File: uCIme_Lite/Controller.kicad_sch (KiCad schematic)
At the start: 35 parts, among them J11 SERIAL_MODE, J12 SERIAL_VOLTAGE_SELECT, Q5 BSS138, Q6 BSS138, Q7 BSS138, Q8 BSS138, U3 AP2204K-ADJ, U4 AP2204K-ADJ, U5 FT230XS, U6 TXB0104D

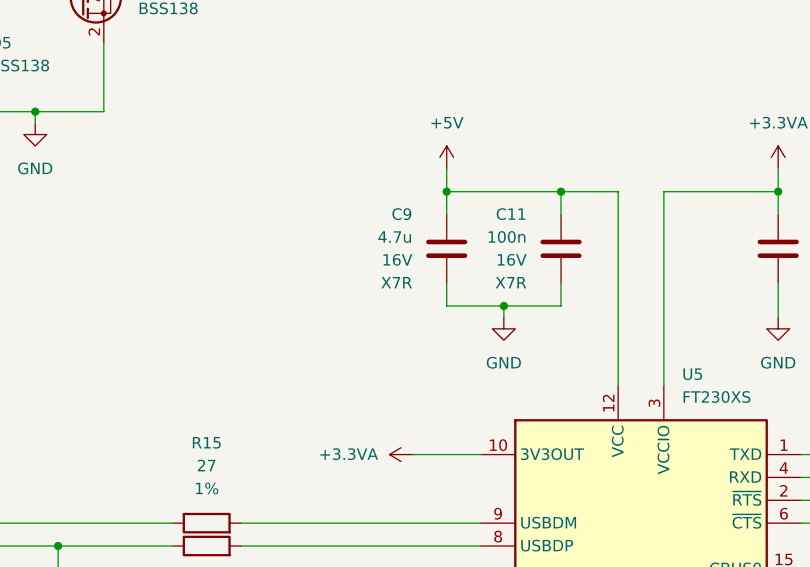
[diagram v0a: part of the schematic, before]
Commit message: lite: Added more part numbers to the schematic. Replaced the FTDI 4.7u capacitor by two 2.2u capacitors to improve the BoM.
Signed-off-by: Adrien Ricciardi <aricciardi@baylibre.com>
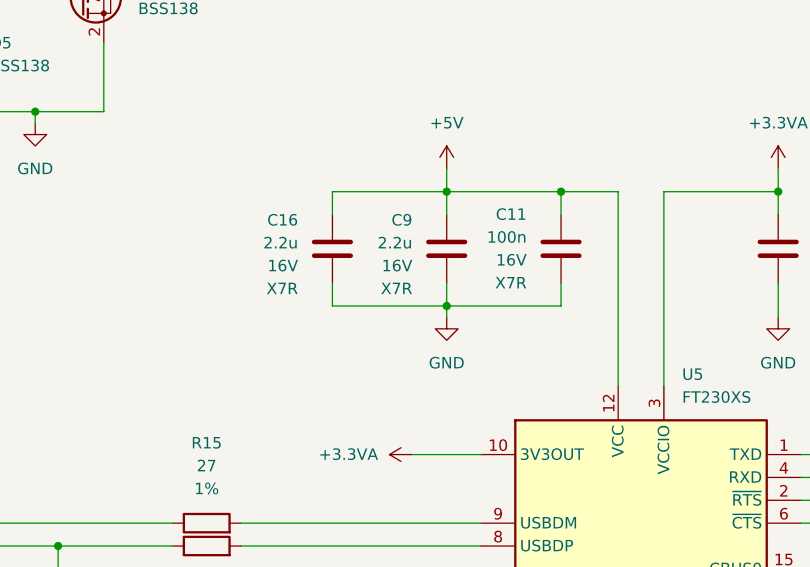
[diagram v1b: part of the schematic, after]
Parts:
- added C16: 2.2u, Capacitor_SMD:C_0603_1608Metric, symbol Device:C
- C6, C7: PartNumber (none) -> CL10C470JB81PNC
- C9: value 4.7u -> 2.2u; footprint Capacitor_SMD:C_0805_2012Metric -> Capacitor_SMD:C_0603_1608Metric; PartNumber (none) -> CL10A225KO8NNNC
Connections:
- net +5V: now also C16.1
- net GND: now also C16.2
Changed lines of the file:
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@@
   (junction (at 74.93 160.02) (diameter 0) (color 0 0 0 0)
   )
+  (junction (at 104.14 77.47) (diameter 0) (color 0 0 0 0)
+  )
   (junction (at 232.41 138.43) (diameter 0) (color 0 0 0 0)
   )
@@
   (junction (at 177.8 52.07) (diameter 0) (color 0 0 0 0)
   )
-  (junction (at 110.49 77.47) (diameter 0) (color 0 0 0 0)
-  )
   (junction (at 26.67 160.02) (diameter 0) (color 0 0 0 0)
   )
@@
     (stroke (width 0) (type default))
   )
+  (wire (pts (xy 91.44 77.47) (xy 104.14 77.47))
+    (stroke (width 0) (type default))
+  )
   (wire (pts (xy 116.84 74.93) (xy 116.84 77.47))
     (stroke (width 0) (type default))
@@
     (stroke (width 0) (type default))
   )
+  (wire (pts (xy 91.44 74.93) (xy 91.44 77.47))
+    (stroke (width 0) (type default))
+  )
   (wire (pts (xy 81.28 101.6) (xy 107.95 101.6))
     (stroke (width 0) (type default))
@@
     (stroke (width 0) (type default))
   )
-  (wire (pts (xy 110.49 77.47) (xy 110.49 78.74))
-    (stroke (width 0) (type default))
-  )
   (wire (pts (xy 36.83 160.02) (xy 26.67 160.02))
     (stroke (width 0) (type default))
@@
     (stroke (width 0) (type default))
   )
-  (wire (pts (xy 110.49 77.47) (xy 116.84 77.47))
+  (wire (pts (xy 104.14 77.47) (xy 116.84 77.47))
     (stroke (width 0) (type default))
   )
@@
     (stroke (width 0) (type default))
   )
+  (wire (pts (xy 91.44 67.31) (xy 91.44 64.77))
+    (stroke (width 0) (type default))
+  )
   (wire (pts (xy 114.3 160.02) (xy 104.14 160.02))
     (stroke (width 0) (type default))
@@
     (stroke (width 0) (type default))
   )
+  (wire (pts (xy 104.14 77.47) (xy 104.14 78.74))
+    (stroke (width 0) (type default))
+  )
   (wire (pts (xy 179.07 118.11) (xy 179.07 106.68))
     (stroke (width 0) (type default))
@@
     (stroke (width 0) (type default))
   )
-  (wire (pts (xy 104.14 77.47) (xy 110.49 77.47))
-    (stroke (width 0) (type default))
-  )
   (wire (pts (xy 58.42 55.88) (xy 58.42 57.15))
     (stroke (width 0) (type default))
@@
   )
   (wire (pts (xy 53.34 101.6) (xy 53.34 109.22))
+    (stroke (width 0) (type default))
+  )
+  (wire (pts (xy 91.44 64.77) (xy 104.14 64.77))
     (stroke (width 0) (type default))
   )
@@
       (effects (font (size 1.27 1.27)) (justify left))
     )
+    (property "PartNumber" "CL10C470JB81PNC" (at 60.96 113.03 0)
+      (effects (font (size 1.27 1.27)) hide)
+    )
     (pin "1")
     (pin "2")
@@
         (path "/6d46d15a-8cd0-4983-b142-8248cafa0b56/85cb8885-4077-4bc3-b1fe-5b247ce2fc7e"
           (reference "C7") (unit 1)
-        )
-      )
-    )
-  )
-  (symbol (lib_id "Device:C") (at 104.14 71.12 0) (unit 1)
-    (in_bom yes) (on_board yes) (dnp no) (fields_autoplaced)
-    (property "Reference" "C9" (at 100.33 67.3099 0)
-      (effects (font (size 1.27 1.27)) (justify right))
-    )
-    (property "Value" "4.7u" (at 100.33 69.8499 0)
-      (effects (font (size 1.27 1.27)) (justify right))
-    )
-    (property "Footprint" "Capacitor_SMD:C_0805_2012Metric" (at 105.1052 74.93 0)
-      (effects (font (size 1.27 1.27)) hide)
-    )
-    (property "Datasheet" "~" (at 104.14 71.12 0)
-      (effects (font (size 1.27 1.27)) hide)
-    )
-    (property "Value2" "16V" (at 100.33 72.3899 0)
-      (effects (font (size 1.27 1.27)) (justify right))
-    )
-    (property "Value3" "X7R" (at 100.33 74.9299 0)
-      (effects (font (size 1.27 1.27)) (justify right))
-    )
-    (pin "1")
-    (pin "2")
-    (instances
-      (project "uCIme_Lite"
-        (path "/6d46d15a-8cd0-4983-b142-8248cafa0b56/85cb8885-4077-4bc3-b1fe-5b247ce2fc7e"
-          (reference "C9") (unit 1)
         )
       )
@@
     )
   )
-  (symbol (lib_id "power:GND") (at 110.49 78.74 0) (unit 1)
-    (in_bom yes) (on_board yes) (dnp no) (fields_autoplaced)
-    (property "Reference" "#PWR0151" (at 110.49 85.09 0)
-      (effects (font (size 1.27 1.27)) hide)
-    )
-    (property "Value" "GND" (at 110.49 83.82 0)
-      (effects (font (size 1.27 1.27)))
-    )
-    (property "Footprint" "" (at 110.49 78.74 0)
-      (effects (font (size 1.27 1.27)) hide)
-    )
-    (property "Datasheet" "" (at 110.49 78.74 0)
+  (symbol (lib_id "power:GND") (at 104.14 78.74 0) (unit 1)
+    (in_bom yes) (on_board yes) (dnp no) (fields_autoplaced)
+    (property "Reference" "#PWR0151" (at 104.14 85.09 0)
+      (effects (font (size 1.27 1.27)) hide)
+    )
+    (property "Value" "GND" (at 104.14 83.82 0)
+      (effects (font (size 1.27 1.27)))
+    )
+    (property "Footprint" "" (at 104.14 78.74 0)
+      (effects (font (size 1.27 1.27)) hide)
+    )
+    (property "Datasheet" "" (at 104.14 78.74 0)
       (effects (font (size 1.27 1.27)) hide)
     )
@@
     (property "Value3" "X7R" (at 49.53 116.8399 0)
       (effects (font (size 1.27 1.27)) (justify right))
+    )
+    (property "PartNumber" "CL10C470JB81PNC" (at 53.34 113.03 0)
+      (effects (font (size 1.27 1.27)) hide)
     )
     (pin "1")
@@
     )
   )
+  (symbol (lib_id "Device:C") (at 104.14 71.12 0) (unit 1)
+    (in_bom yes) (on_board yes) (dnp no) (fields_autoplaced)
+    (property "Reference" "C9" (at 100.33 67.945 0)
+      (effects (font (size 1.27 1.27)) (justify right))
+    )
+    (property "Value" "2.2u" (at 100.33 70.485 0)
+      (effects (font (size 1.27 1.27)) (justify right))
+    )
+    (property "Footprint" "Capacitor_SMD:C_0603_1608Metric" (at 105.1052 74.93 0)
+      (effects (font (size 1.27 1.27)) hide)
+    )
+    (property "Datasheet" "~" (at 104.14 71.12 0)
+      (effects (font (size 1.27 1.27)) hide)
+    )
+    (property "Value2" "16V" (at 100.33 73.025 0)
+      (effects (font (size 1.27 1.27)) (justify right))
+    )
+    (property "Value3" "X7R" (at 100.33 75.565 0)
+      (effects (font (size 1.27 1.27)) (justify right))
+    )
+    (property "PartNumber" "CL10A225KO8NNNC" (at 104.14 71.12 0)
+      (effects (font (size 1.27 1.27)) hide)
+    )
+    (pin "1")
+    (pin "2")
+    (instances
+      (project "uCIme_Lite"
+        (path "/6d46d15a-8cd0-4983-b142-8248cafa0b56/85cb8885-4077-4bc3-b1fe-5b247ce2fc7e"
+          (reference "C9") (unit 1)
+        )
+      )
+    )
+  )
   (symbol (lib_id "power:GND") (at 45.72 171.45 0) (unit 1)
     (in_bom yes) (on_board yes) (dnp no) (fields_autoplaced)
@@
         )
       )
+    )
+  )
+  (symbol (lib_id "Device:C") (at 91.44 71.12 0) (unit 1)
+    (in_bom yes) (on_board yes) (dnp no) (fields_autoplaced)
+    (property "Reference" "C16" (at 87.63 67.945 0)
+      (effects (font (size 1.27 1.27)) (justify right))
+    )
+    (property "Value" "2.2u" (at 87.63 70.485 0)
+      (effects (font (size 1.27 1.27)) (justify right))
+    )
+    (property "Footprint" "Capacitor_SMD:C_0603_1608Metric" (at 92.4052 74.93 0)
+      (effects (font (size 1.27 1.27)) hide)
+    )
+    (property "Datasheet" "~" (at 91.44 71.12 0)
+      (effects (font (size 1.27 1.27)) hide)
+    )
+    (property "Value2" "16V" (at 87.63 73.025 0)
+      (effects (font (size 1.27 1.27)) (justify right))
+    )
+    (property "Value3" "X7R" (at 87.63 75.565 0)
+      (effects (font (size 1.27 1.27)) (justify right))
+    )
+    (property "PartNumber" "CL10A225KO8NNNC" (at 91.44 71.12 0)
+      (effects (font (size 1.27 1.27)) hide)
+    )
+    (pin "1")
+    (pin "2")
+    (instances
+      (project "uCIme_Lite"
+        (path "/6d46d15a-8cd0-4983-b142-8248cafa0b56/85cb8885-4077-4bc3-b1fe-5b247ce2fc7e"
+          (reference "C16") (unit 1)
+        )
+      )

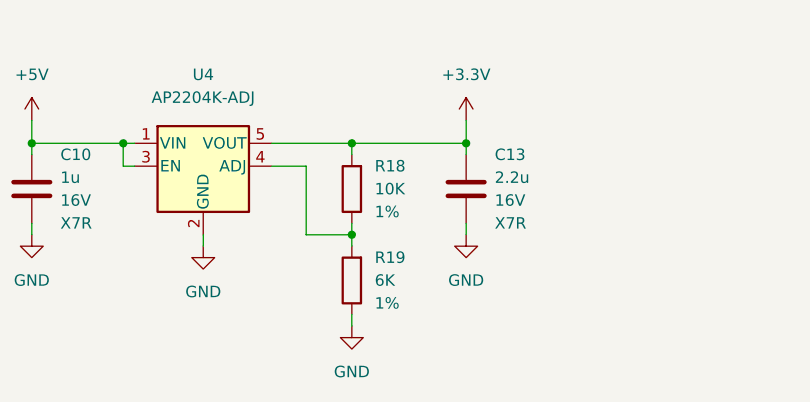
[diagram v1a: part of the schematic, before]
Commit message: lite: Added to schematic all missing part numbers but the pin header ones.
Signed-off-by: Adrien Ricciardi <aricciardi@baylibre.com>
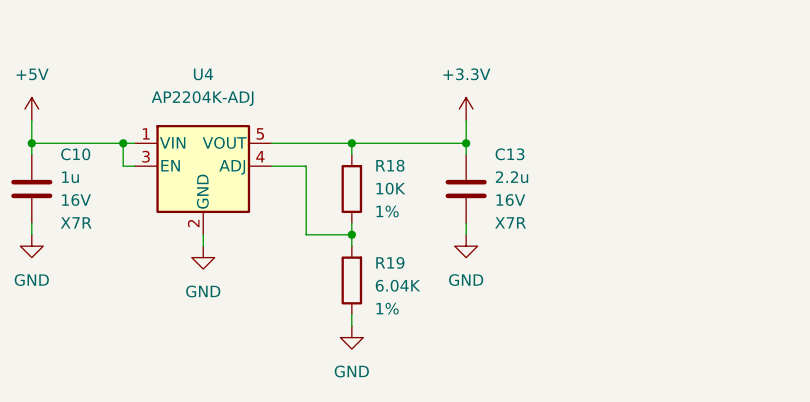
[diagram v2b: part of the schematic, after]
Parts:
- C11, C12, C14, C15: PartNumber (none) -> CL10B104KO8NNNC
- D4, D5: footprint (none) -> LED_SMD:LED_0805_2012Metric; PartNumber (none) -> 150080SS75000
- J11: footprint (none) -> Connector_PinHeader_2.54mm:PinHeader_1x03_P2.54mm_Horizontal
- J12: footprint (none) -> Connector_PinHeader_2.54mm:PinHeader_2x03_P2.54mm_Horizontal
- R11, R20: footprint Resistor_SMD:R_1206_3216Metric -> Resistor_SMD:R_0603_1608Metric; PartNumber (none) -> RC0603FR-07100KL
- R12, R21: footprint Resistor_SMD:R_1206_3216Metric -> Resistor_SMD:R_0603_1608Metric; PartNumber (none) -> RNCP0603FTD10K0
- R13, R18: PartNumber (none) -> RNCP0603FTD10K0
- R14: PartNumber (none) -> RC0603FR-0722KL
- R17, R22: PartNumber (none) -> RC1206JR-07240RL
- R19: value 6K -> 6.04K; PartNumber (none) -> RC0603FR-076K04L
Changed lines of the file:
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@@
       (effects (font (size 1.27 1.27)) (justify right))
+    )
+    (property "PartNumber" "RC0603FR-0722KL" (at 62.23 175.26 0)
+      (effects (font (size 1.27 1.27)) hide)
     )
     (pin "1")
@@
     (property "Value3" "X7R" (at 212.09 60.9599 0)
       (effects (font (size 1.27 1.27)) (justify left))
+    )
+    (property "PartNumber" "CL10B104KO8NNNC" (at 208.28 57.15 0)
+      (effects (font (size 1.27 1.27)) hide)
     )
     (pin "1")
@@
       (effects (font (size 1.27 1.27)) (justify right))
     )
+    (property "PartNumber" "RNCP0603FTD10K0" (at 139.7 165.1 0)
+      (effects (font (size 1.27 1.27)) hide)
+    )
     (pin "1")
     (pin "2")
@@
       (effects (font (size 1.27 1.27)) hide)
     )
-    (property "PartNumber" "" (at 82.55 34.29 0)
+    (property "PartNumber" "RC1206JR-07240RL" (at 82.55 34.29 0)
       (effects (font (size 1.27 1.27)) hide)
     )
@@
       (effects (font (size 1.27 1.27)) (justify right))
     )
+    (property "PartNumber" "CL10B104KO8NNNC" (at 177.8 57.15 0)
+      (effects (font (size 1.27 1.27)) hide)
+    )
     (pin "1")
     (pin "2")
@@
   (symbol (lib_id "Device:R") (at 139.7 175.26 180) (unit 1)
     (in_bom yes) (on_board yes) (dnp no) (fields_autoplaced)
-    (property "Reference" "R19" (at 142.24 172.7199 0)
-      (effects (font (size 1.27 1.27)) (justify right))
-    )
-    (property "Value" "6K" (at 142.24 175.2599 0)
+    (property "Reference" "R19" (at 142.24 173.355 0)
+      (effects (font (size 1.27 1.27)) (justify right))
+    )
+    (property "Value" "6.04K" (at 142.24 175.895 0)
       (effects (font (size 1.27 1.27)) (justify right))
     )
@@
       (effects (font (size 1.27 1.27)) hide)
     )
-    (property "Value2" "1%" (at 142.24 177.7999 0)
-      (effects (font (size 1.27 1.27)) (justify right))
+    (property "Value2" "1%" (at 142.24 178.435 0)
+      (effects (font (size 1.27 1.27)) (justify right))
+    )
+    (property "PartNumber" "RC0603FR-076K04L" (at 139.7 175.26 0)
+      (effects (font (size 1.27 1.27)) hide)
     )
     (pin "1")
@@
       (effects (font (size 1.27 1.27)) (justify right))
     )
-    (property "Footprint" "" (at 153.67 36.83 0)
+    (property "Footprint" "Connector_PinHeader_2.54mm:PinHeader_1x03_P2.54mm_Horizontal" (at 153.67 36.83 0)
       (effects (font (size 1.27 1.27)) hide)
     )
@@
       (effects (font (size 1.27 1.27)) (justify left))
     )
+    (property "PartNumber" "CL10B104KO8NNNC" (at 140.97 71.12 0)
+      (effects (font (size 1.27 1.27)) hide)
+    )
     (pin "1")
     (pin "2")
@@
       (effects (font (size 1.27 1.27)) (justify left))
     )
-    (property "Footprint" "Resistor_SMD:R_1206_3216Metric" (at 42.418 54.61 90)
+    (property "Footprint" "Resistor_SMD:R_0603_1608Metric" (at 42.418 54.61 90)
       (effects (font (size 1.27 1.27)) hide)
     )
@@
       (effects (font (size 1.27 1.27)) hide)
     )
-    (property "PartNumber" "" (at 40.64 54.61 0)
+    (property "PartNumber" "RC0603FR-07100KL" (at 40.64 54.61 0)
       (effects (font (size 1.27 1.27)) hide)
     )
@@
       (effects (font (size 1.27 1.27)))
     )
-    (property "Footprint" "" (at 232.41 52.07 0)
+    (property "Footprint" "Connector_PinHeader_2.54mm:PinHeader_2x03_P2.54mm_Horizontal" (at 232.41 52.07 0)
       (effects (font (size 1.27 1.27)) hide)
     )
@@
       (effects (font (size 1.27 1.27)) (justify right))
     )
-    (property "Footprint" "Resistor_SMD:R_1206_3216Metric" (at 51.308 38.1 90)
+    (property "Footprint" "Resistor_SMD:R_0603_1608Metric" (at 51.308 38.1 90)
       (effects (font (size 1.27 1.27)) hide)
     )
@@
       (effects (font (size 1.27 1.27)) hide)
     )
-    (property "PartNumber" "" (at 49.53 38.1 0)
+    (property "PartNumber" "RNCP0603FTD10K0" (at 49.53 38.1 0)
       (effects (font (size 1.27 1.27)) hide)
     )
@@
       (effects (font (size 1.27 1.27)))
     )
-    (property "Footprint" "" (at 256.54 129.54 0)
+    (property "Footprint" "LED_SMD:LED_0805_2012Metric" (at 256.54 129.54 0)
       (effects (font (size 1.27 1.27)) hide)
     )
@@
       (effects (font (size 1.27 1.27)) hide)
     )
+    (property "PartNumber" "150080SS75000" (at 256.54 129.54 0)
+      (effects (font (size 1.27 1.27)) hide)
+    )
     (pin "1")
     (pin "2")
@@
       (effects (font (size 1.27 1.27)))
     )
-    (property "Footprint" "" (at 73.66 34.29 0)
+    (property "Footprint" "LED_SMD:LED_0805_2012Metric" (at 73.66 34.29 0)
       (effects (font (size 1.27 1.27)) hide)
     )
     (property "Datasheet" "~" (at 73.66 34.29 0)
+      (effects (font (size 1.27 1.27)) hide)
+    )
+    (property "PartNumber" "150080SS75000" (at 73.66 34.29 0)
       (effects (font (size 1.27 1.27)) hide)
     )
@@
       (effects (font (size 1.27 1.27)) (justify right))
     )
+    (property "PartNumber" "CL10B104KO8NNNC" (at 116.84 71.12 0)
+      (effects (font (size 1.27 1.27)) hide)
+    )
     (pin "1")
     (pin "2")
@@
       (effects (font (size 1.27 1.27)) (justify right))
     )
-    (property "Footprint" "Resistor_SMD:R_1206_3216Metric" (at 234.188 133.35 90)
+    (property "Footprint" "Resistor_SMD:R_0603_1608Metric" (at 234.188 133.35 90)
       (effects (font (size 1.27 1.27)) hide)
     )
@@
       (effects (font (size 1.27 1.27)) hide)
     )
-    (property "PartNumber" "" (at 232.41 133.35 0)
+    (property "PartNumber" "RNCP0603FTD10K0" (at 232.41 133.35 0)
       (effects (font (size 1.27 1.27)) hide)
     )
@@
       (effects (font (size 1.27 1.27)) (justify left))
     )
-    (property "Footprint" "Resistor_SMD:R_1206_3216Metric" (at 225.298 149.86 90)
+    (property "Footprint" "Resistor_SMD:R_0603_1608Metric" (at 225.298 149.86 90)
       (effects (font (size 1.27 1.27)) hide)
     )
@@
       (effects (font (size 1.27 1.27)) hide)
     )
-    (property "PartNumber" "" (at 223.52 149.86 0)
+    (property "PartNumber" "RC0603FR-07100KL" (at 223.52 149.86 0)
       (effects (font (size 1.27 1.27)) hide)
     )
@@
       (effects (font (size 1.27 1.27)) (justify right))
     )
+    (property "PartNumber" "RNCP0603FTD10K0" (at 62.23 165.1 0)
+      (effects (font (size 1.27 1.27)) hide)
+    )
     (pin "1")
     (pin "2")
@@
       (effects (font (size 1.27 1.27)) hide)
     )
-    (property "PartNumber" "" (at 265.43 129.54 0)
-      (effects (font (size 1.27 1.27)) hide)
-    )
+    (property "PartNumber" "RC1206JR-07240RL" (at 265.43 129.54 0)
+      (effects (font (size 1.27 1.27)) hide)
+    )
